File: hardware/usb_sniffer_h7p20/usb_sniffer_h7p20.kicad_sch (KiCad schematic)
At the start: 99 parts, among them J1 FPGA_JTAG, J4 USB_C_Receptacle_USB2.0_16P, J5 FFC-40P-0.5mm,NC, J6 Trigger, U1 H7P20N0L128-M3H1, U6 P25Q32SH-SSH-IT, U7 CY7C68013A-56LTX, U8 24C64BN, U9 CJ3439KDW, X1 XO32,26M,NC, Y2 24M

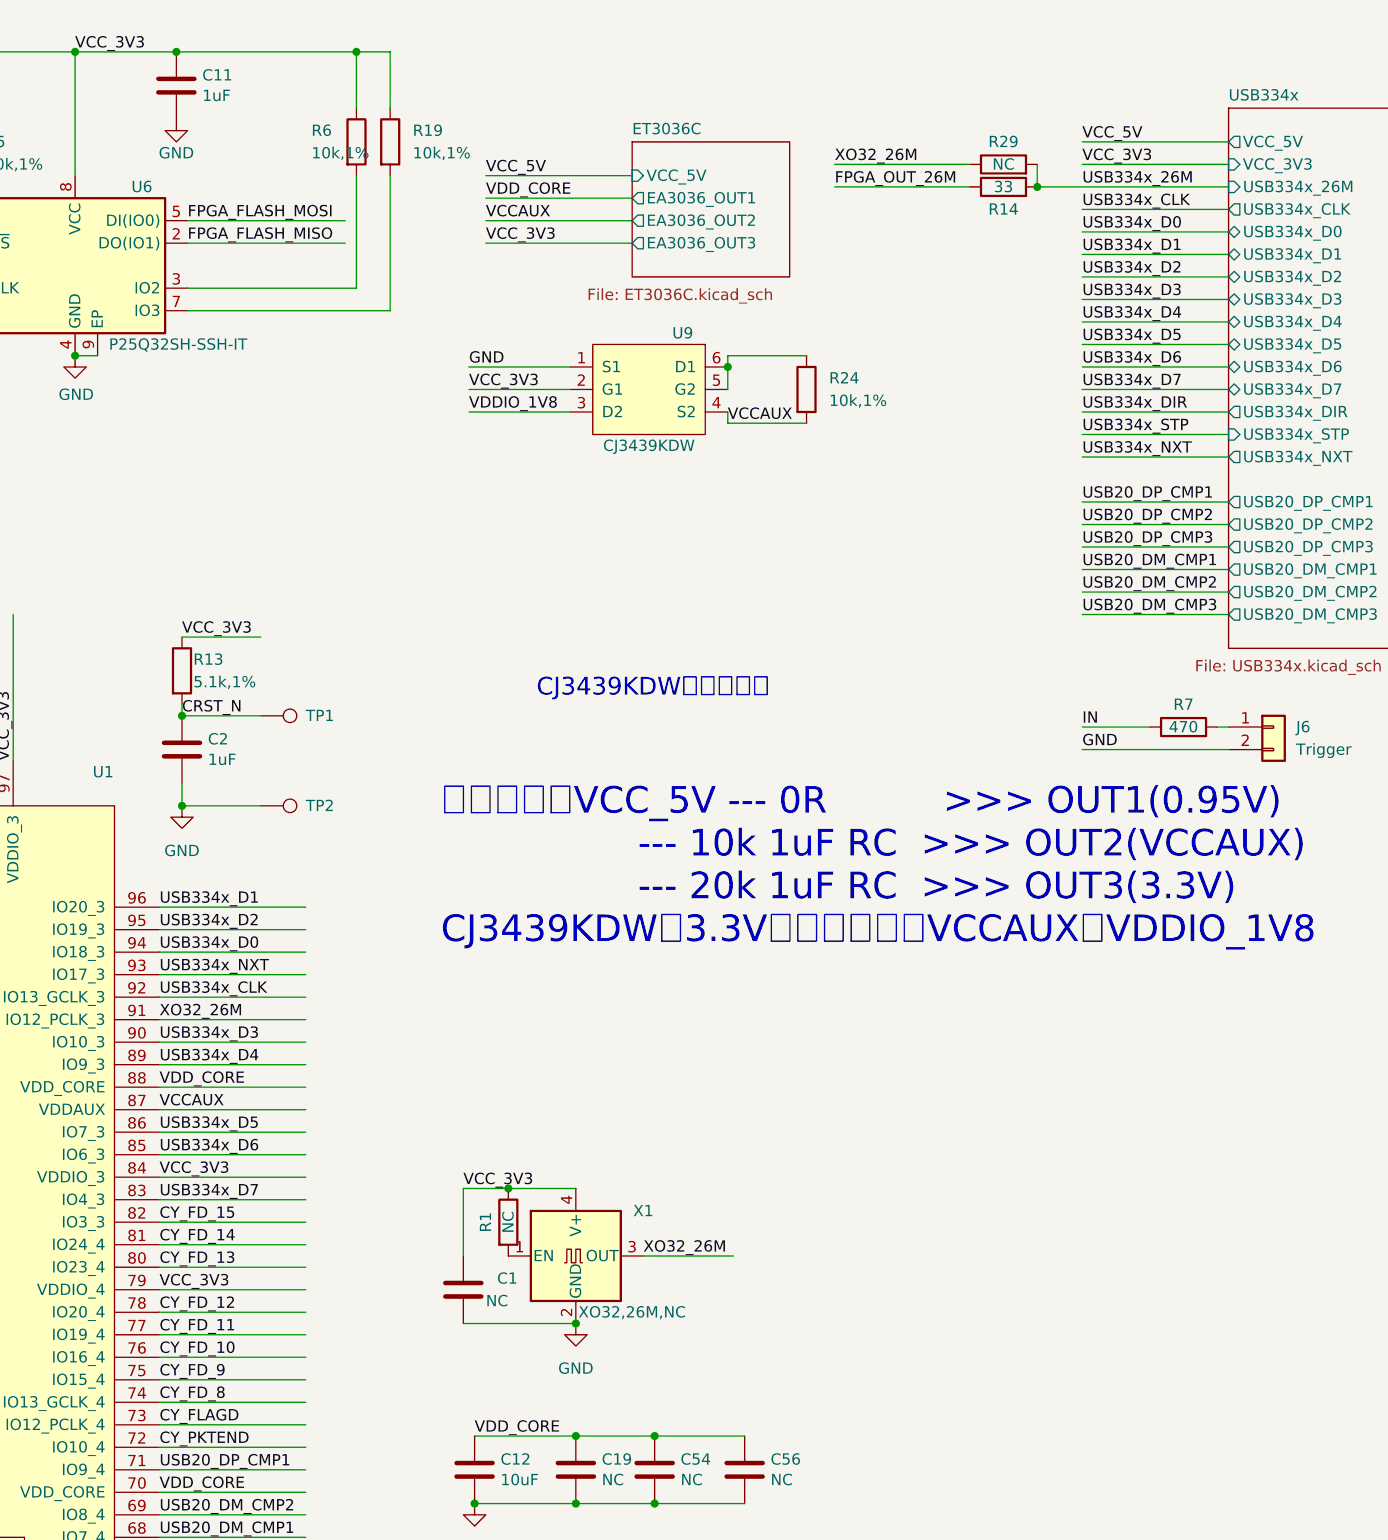
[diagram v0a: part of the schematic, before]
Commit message: [usb_sniffer_h7p20] 移除NC器件，更换LM2903A-VR，双螺丝孔固定
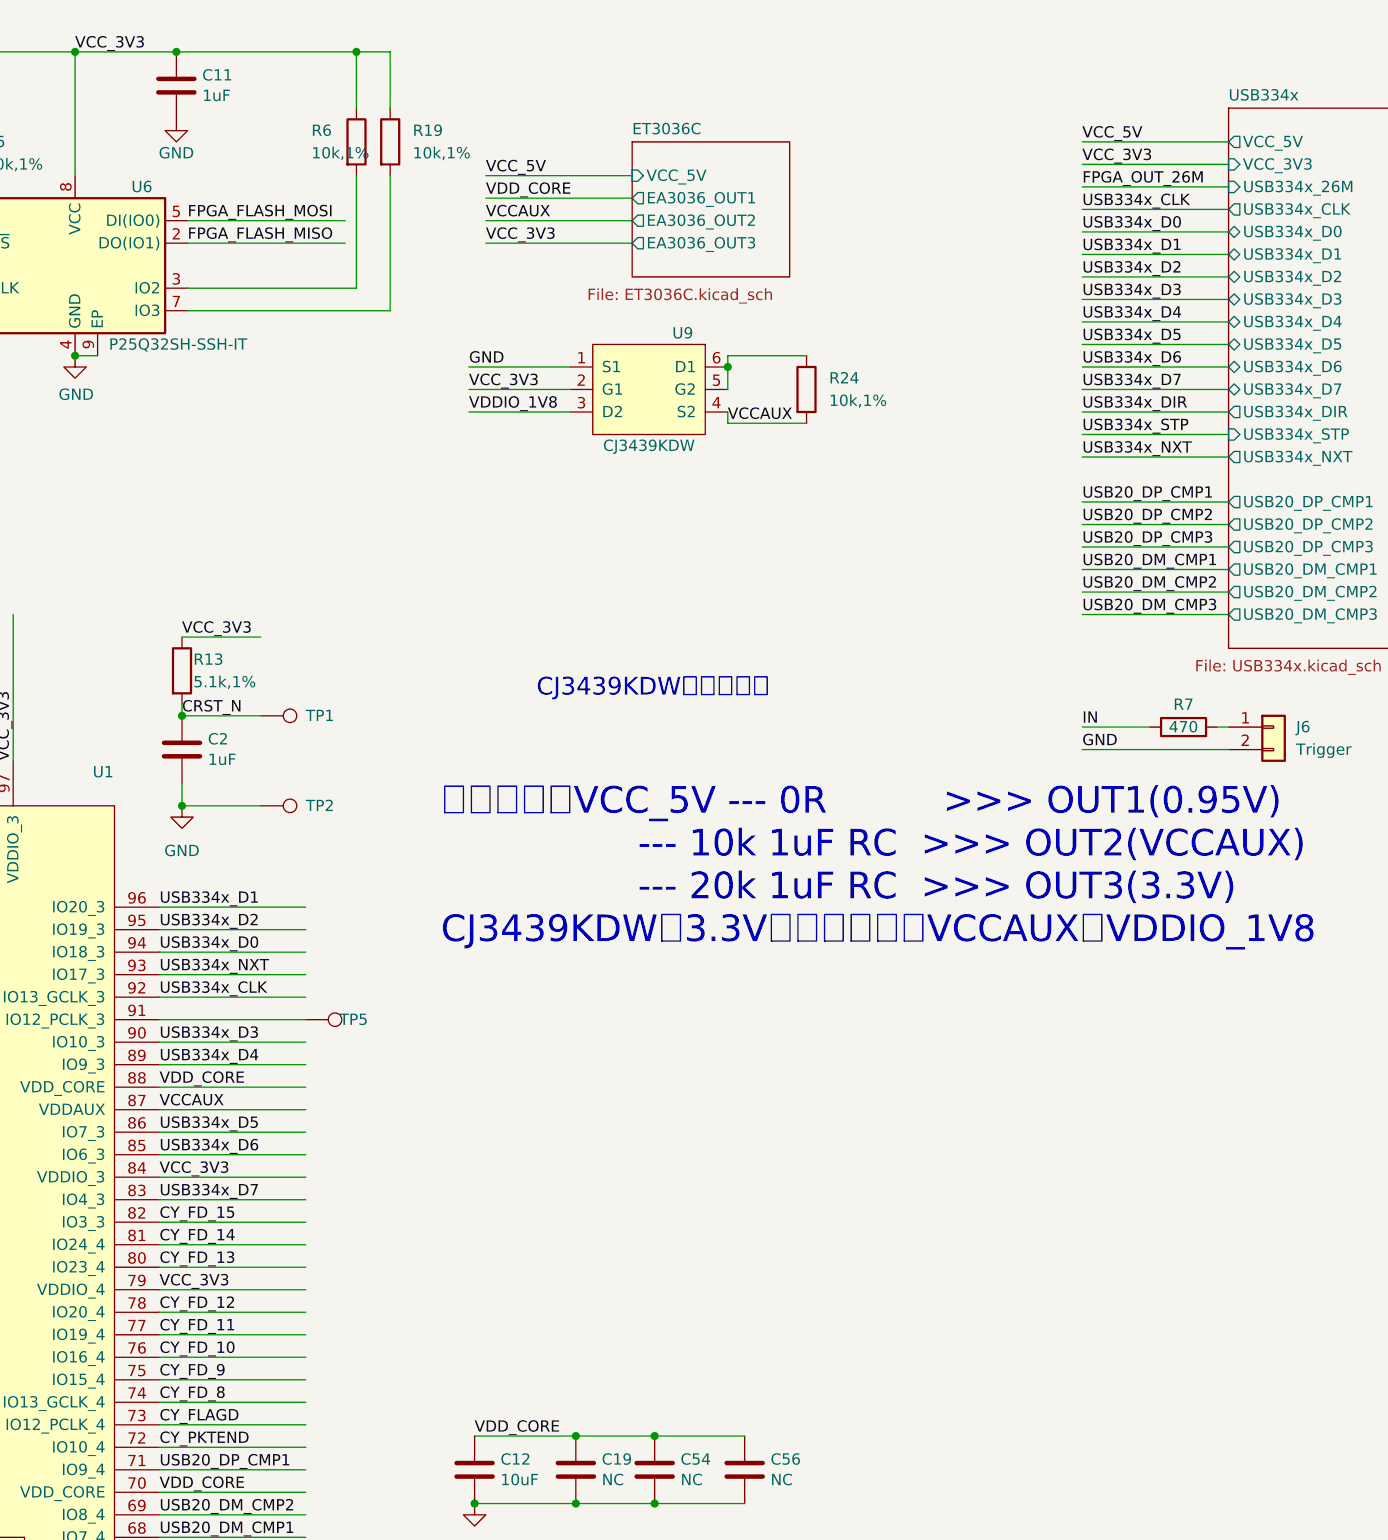
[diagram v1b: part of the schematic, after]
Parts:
- removed C1: NC, Capacitor_SMD:C_0402_1005Metric, symbol Device:C
- removed R1, R29: NC, Resistor_SMD:R_0402_1005Metric, symbol Device:R
- removed R14: 33, Resistor_SMD:R_0402_1005Metric, symbol Device:R
- removed X1: XO32,26M,NC, vllogic:OSC_3225, symbol Oscillator:XO32
- added TP5: TestPoint, vllogic:TestPoint_Pad_D0.3mm, symbol Connector:TestPoint
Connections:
- net XO32_26M: no longer names the net of U1.91 (IO12_PCLK_3)
- net XO32_26M: now also TP5.1

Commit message: [usb_sniffer_h7p20] 优化USB封装精度，优化定位孔精度
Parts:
- J4: footprint Connector_USB:USB_C_Receptacle_GCT_USB4105-xx-A_16P_TopMnt_Horizontal -> vllogic:USB_C_Receptacle_16P
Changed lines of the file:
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@@
       (effects (font (size 1.27 1.27)))
     )
-    (property "Footprint" "Connector_USB:USB_C_Receptacle_GCT_USB4105-xx-A_16P_TopMnt_Horizontal" (at 34.29 36.83 0)
+    (property "Footprint" "vllogic:USB_C_Receptacle_16P" (at 34.29 36.83 0)
       (effects (font (size 1.27 1.27)) hide)
     )

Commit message: [usb_sniffer_h7p20] production_files.2025620
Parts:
- U6: value P25Q32SH-SSH-IT -> ZB25VQ16CTJG
- U8: value 24C64BN -> 24C32
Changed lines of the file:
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@@
       (effects (font (size 1.27 1.27)) (justify left))
     )
-    (property "Value" "24C64BN" (at 44.45 226.06 0)
+    (property "Value" "24C32" (at 44.45 226.06 0)
       (effects (font (size 1.27 1.27)) (justify left))
     )
@@
       (effects (font (size 1.27 1.27)) (justify left))
     )
-    (property "Value" "P25Q32SH-SSH-IT" (at 240.665 49.53 0)
-      (effects (font (size 1.27 1.27)) (justify left))
-    )
+    (property "Value" "ZB25VQ16CTJG" (at 240.665 49.53 0)
+      (effects (font (size 1.27 1.27)) (justify left))
+    )

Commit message: 将USB3343替换为CH132C，ULPI时钟由FPGA产生
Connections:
- net FPGA_OUT_26M: no longer names the net of U1.104 (IO27_GCLK_2)
- no-connect marks 6 -> 7
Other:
- sheet USB334x ports: added none; removed USB334x_26M

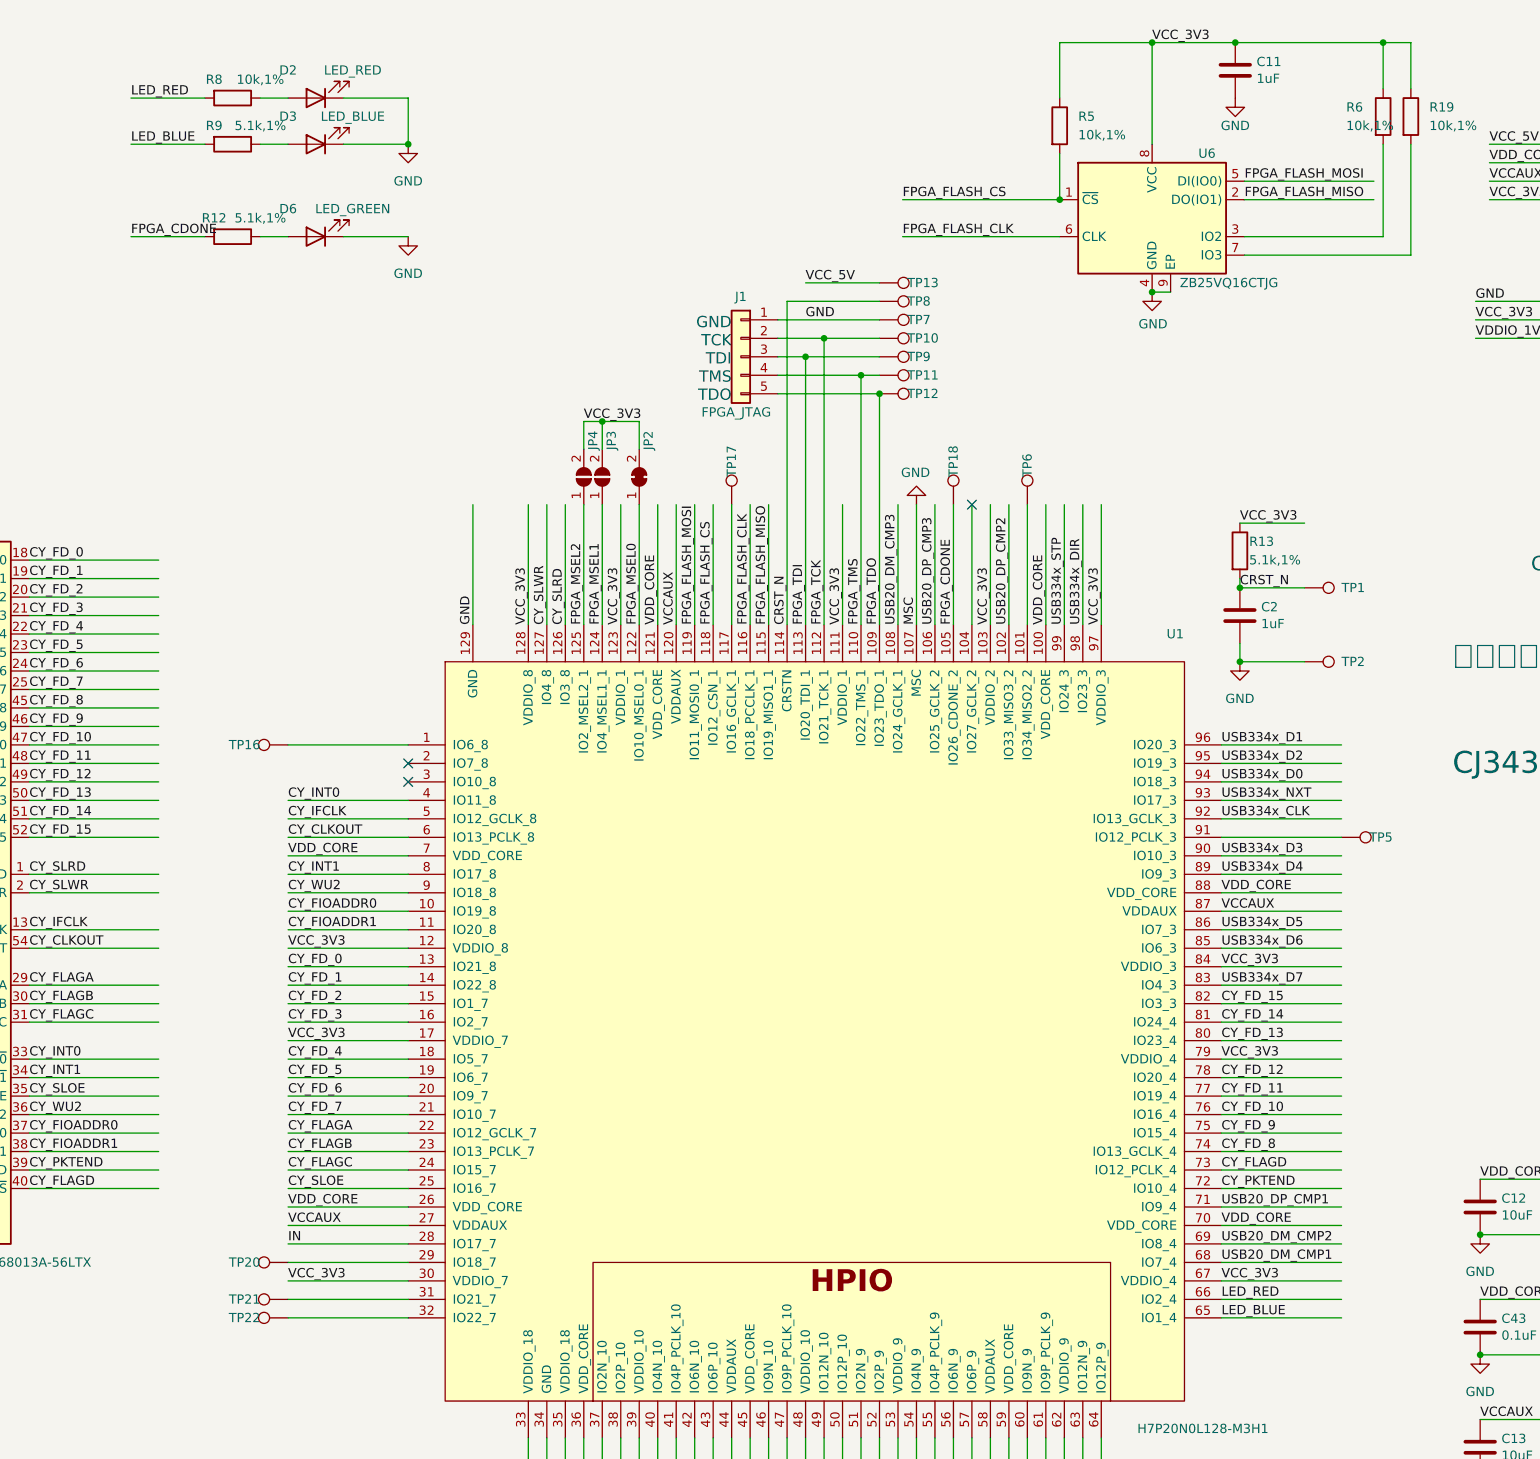
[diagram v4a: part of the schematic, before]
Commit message: [usb_sniffer_h7p20] 适配铝合金外壳、更换CH132C
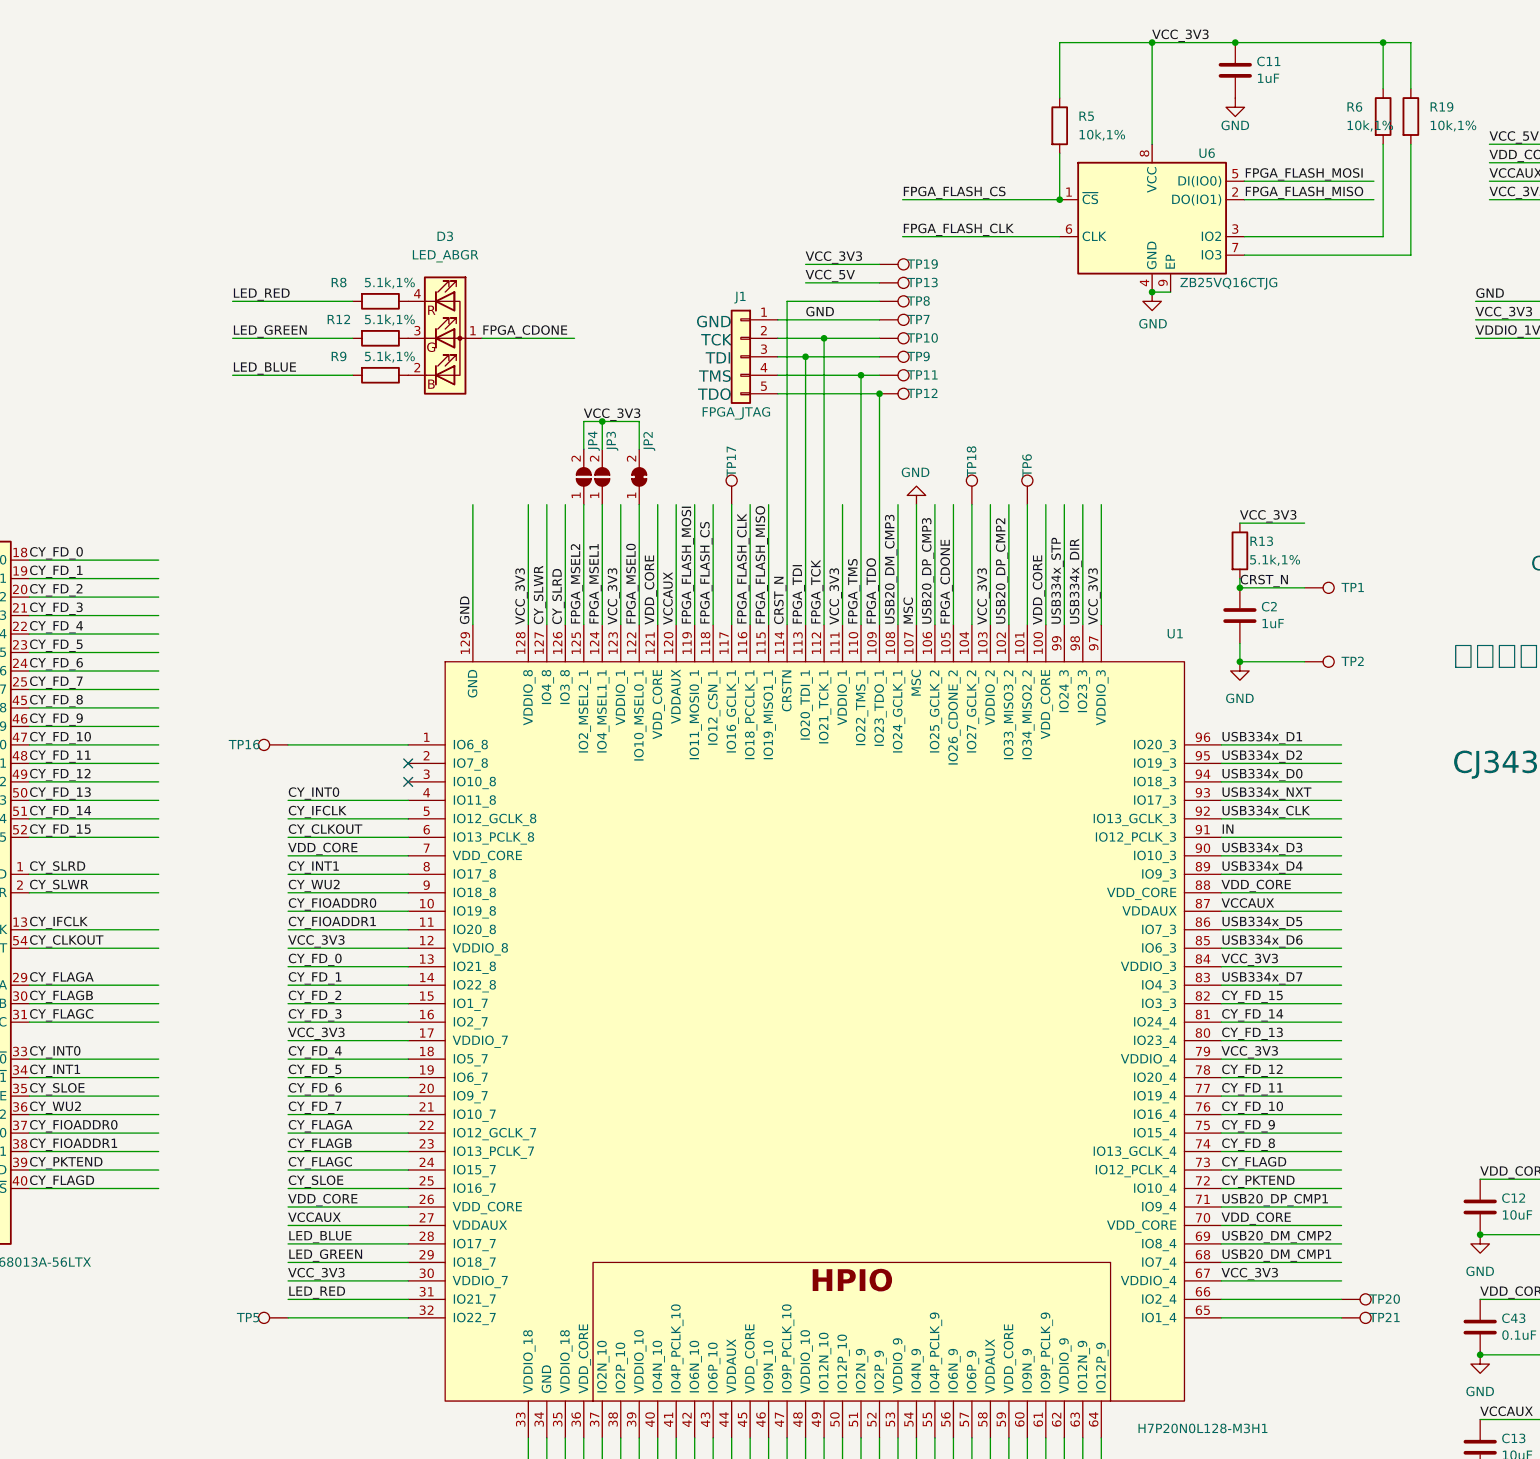
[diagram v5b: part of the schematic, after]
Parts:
- removed D2: LED_RED, LED_SMD:LED_0603_1608Metric, symbol Device:LED
- removed D3: LED_BLUE, LED_SMD:LED_0603_1608Metric, symbol Device:LED
- removed D6: LED_GREEN, LED_SMD:LED_0603_1608Metric, symbol Device:LED
- removed TP22: TestPoint, vllogic:TestPoint_Pad_D0.3mm, symbol Connector:TestPoint
- added D3: LED_ABGR, LED_SMD:LED_RGB_Everlight_EASV3015RGBA0_Horizontal, symbol Device:LED_ABGR
- added TP19: TestPoint, vllogic:TestPoint_Pad_D0.75mm, symbol Connector:TestPoint
- R8: value 10k,1% -> 5.1k,1%
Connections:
- net FPGA_CDONE: now also D3.1 (A); no longer R12.2, TP18.1
- net IN: now also U1.91 (IO12_PCLK_3); no longer U1.28 (IO17_7)
- net LED_BLUE: now also U1.28 (IO17_7); no longer U1.65 (IO1_4)
- net LED_RED: now also U1.31 (IO21_7); no longer U1.66 (IO2_4)
- net VCC_3V3: now also TP19.1
- net at R8.1: now also D3.4 (RK)
- net at R12.1: now also D3.3 (GK)
- net at R9.1: now also D3.2 (BK)
- net at TP21.1: now also U1.65 (IO1_4); no longer U1.31 (IO21_7)
- net at U1.32 (IO22_7): now also TP5.1
- net at TP20.1: now also U1.66 (IO2_4); no longer U1.29 (IO18_7)
- net at U1.104 (IO27_GCLK_2): now also TP18.1
- new net LED_GREEN: R12.2, U1.29 (IO18_7)
- no-connect marks 7 -> 6
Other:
- moved on the sheet: R12, TP18, TP5

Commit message: [usb_sniffer_h7p20] 待审查
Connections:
- net IN: now also U1.89 (IO9_3); no longer U1.91 (IO12_PCLK_3)
- net USB334x_D0: now also U1.93 (IO17_3); no longer U1.94 (IO18_3)
- net USB334x_D3: now also U1.94 (IO18_3); no longer U1.90 (IO10_3)
- net USB334x_D4: now also U1.90 (IO10_3); no longer U1.89 (IO9_3)
- net USB334x_DIR: now also U1.91 (IO12_PCLK_3); no longer U1.98 (IO23_3)
- net USB334x_NXT: now also U1.99 (IO24_3); no longer U1.93 (IO17_3)
- net USB334x_STP: now also U1.98 (IO23_3); no longer U1.99 (IO24_3)
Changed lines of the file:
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@@
 	)
 	(label "IN"
-		(at 246.38 125.73 0)
+		(at 246.38 130.81 0)
 		(effects
 			(font
@@
 	)
 	(label "USB334x_NXT"
-		(at 246.38 120.65 0)
+		(at 224.79 96.52 90)
 		(effects
 			(font
@@
 	)
 	(label "USB334x_STP"
-		(at 224.79 96.52 90)
+		(at 227.33 96.52 90)
 		(effects
 			(font
@@
 	)
 	(label "USB334x_D3"
-		(at 246.38 128.27 0)
+		(at 246.38 118.11 0)
 		(effects
 			(font
@@
 	)
 	(label "USB334x_DIR"
-		(at 227.33 96.52 90)
+		(at 246.38 125.73 0)
 		(effects
 			(font
@@
 	)
 	(label "USB334x_D4"
-		(at 246.38 130.81 0)
+		(at 246.38 128.27 0)
 		(effects
 			(font
@@
 	)
 	(label "USB334x_D0"
-		(at 246.38 118.11 0)
-		(effects
-			(font
+		(at 246.38 120.65 0)
+		(effects
+			(font

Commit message: [usb_sniffer_h7p20] 20250813 打样
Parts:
- R8: value 5.1k,1% -> 10k,1%
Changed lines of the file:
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@@
 			)
 		)
-		(property "Value" "5.1k,1%"
+		(property "Value" "10k,1%"
 			(at 132.08 49.53 90)
 			(effects
